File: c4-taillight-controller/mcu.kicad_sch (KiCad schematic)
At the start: 8 parts, among them J1 Conn_01x05_Pin, M1 MDBT50Q-1MV2, X1 32.768KHz

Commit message: 8/17/2026 added MCU
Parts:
- removed C2, C3: 12pF, symbol Device:C
- removed C4, C5, C6: 10uF, symbol Device:C
- removed J1: Conn_01x05_Pin, symbol Connector:Conn_01x05_Pin
- removed M1: MDBT50Q-1MV2, symbol MDBT50Q:MDBT50Q_52840
- removed X1: 32.768KHz, symbol Device:Crystal
- added C10, C11, C9: 10uF, symbol Device:C
- added C7, C8: 12pF, symbol Device:C
- added J2: Conn_01x05_Pin, symbol Connector:Conn_01x05_Pin
- added M2: MDBT50Q-1MV2, symbol MDBT50Q:MDBT50Q_52840
- added X2: 32.768KHz, symbol Device:Crystal
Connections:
- net D+: now also M2.35 (D+)
- net D-: now also M2.34 (D-)
- net GND: now also C10.2, C11.1, C7.1, C8.1, C9.1, J2.1 (Pin_1), M2.1 (GND), M2.15 (GND), M2.2 (GND), M2.33 (GND), M2.55 (GND)
- net RESET: now also J2.2 (Pin_2), M2.40 (P0.18/RESET)
- net SWDCLK: now also J2.4 (Pin_4), M2.53 (SWDCLK)
- net SWDIO: now also J2.3 (Pin_3), M2.51 (SWDIO)
- net VBUS (+5V): now also C11.2, M2.32 (VBUS)
- net VDD HV (+5V): now also C10.1, M2.30 (VDDH)
- net VDD_RF: now also C9.2, J2.5 (Pin_5), M2.28 (VDD)
- net XL1: now also C7.2, M2.17 (P0.00/XL1), X2.2
- net XL2: now also C8.2, M2.18 (P0.01/XL2), X2.1
- new net DCCH: M2.31 (DCCH)
- new net P0.02/AIN0: M2.11 (P0.02/AIN0)
- new net P0.03/AIN1: M2.9 (P0.03/AIN1)
- new net P0.04/AIN2: M2.20 (P0.04/AIN2)
- new net P0.05/AIN3: M2.21 (P0.05/AIN3)
- new net P0.06: M2.22 (P0.06)
- new net P0.07: M2.23 (P0.07)
- new net P0.08: M2.24 (P0.08)
- new net P0.09/NFC1: M2.52 (P0.09/NFC1)
- new net P0.10/NFC2: M2.54 (P0.10/NFC2)
- new net P0.11: M2.27 (P0.11)
- new net P0.12: M2.29 (P0.12)
- new net P0.13: M2.37 (P0.13)
- new net P0.14: M2.36 (P0.14)
- new net P0.15: M2.39 (P0.15)
- new net P0.16: M2.38 (P0.16)
- new net P0.17: M2.41 (P0.17)
- new net P0.19: M2.42 (P0.19)
- new net P0.20: M2.44 (P0.20)
- new net P0.21: M2.43 (P0.21)
- new net P0.22: M2.46 (P0.22)
- new net P0.23: M2.45 (P0.23)
- new net P0.24: M2.48 (P0.24)
- new net P0.25: M2.49 (P0.25)
- new net P0.26: M2.19 (P0.26)
- new net P0.27: M2.16 (P0.27)
- new net P0.28/AIN4: M2.13 (P0.28/AIN4)
- new net P0.29/AIN5: M2.10 (P0.29/AIN5)
- new net P0.30/AIN6: M2.14 (P0.30/AIN6)
- new net P0.31/AIN7: M2.12 (P0.31/AIN7)
- new net P1.00: M2.47 (P1.00)
- new net P1.01: M2.61 (P1.01)
- new net P1.02: M2.50 (P1.02)
- new net P1.03: M2.60 (P1.03)
- new net P1.04: M2.56 (P1.04)
- new net P1.05: M2.59 (P1.05)
- new net P1.06: M2.57 (P1.06)
- new net P1.07: M2.58 (P1.07)
- new net P1.08: M2.25 (P1.08)
- new net P1.09: M2.26 (P1.09)
- new net P1.10: M2.3 (P1.10)
- new net P1.11: M2.4 (P1.11)
- new net P1.12: M2.5 (P1.12)
- new net P1.13: M2.6 (P1.13)
- new net P1.14: M2.7 (P1.14)
- new net P1.15: M2.8 (P1.15)

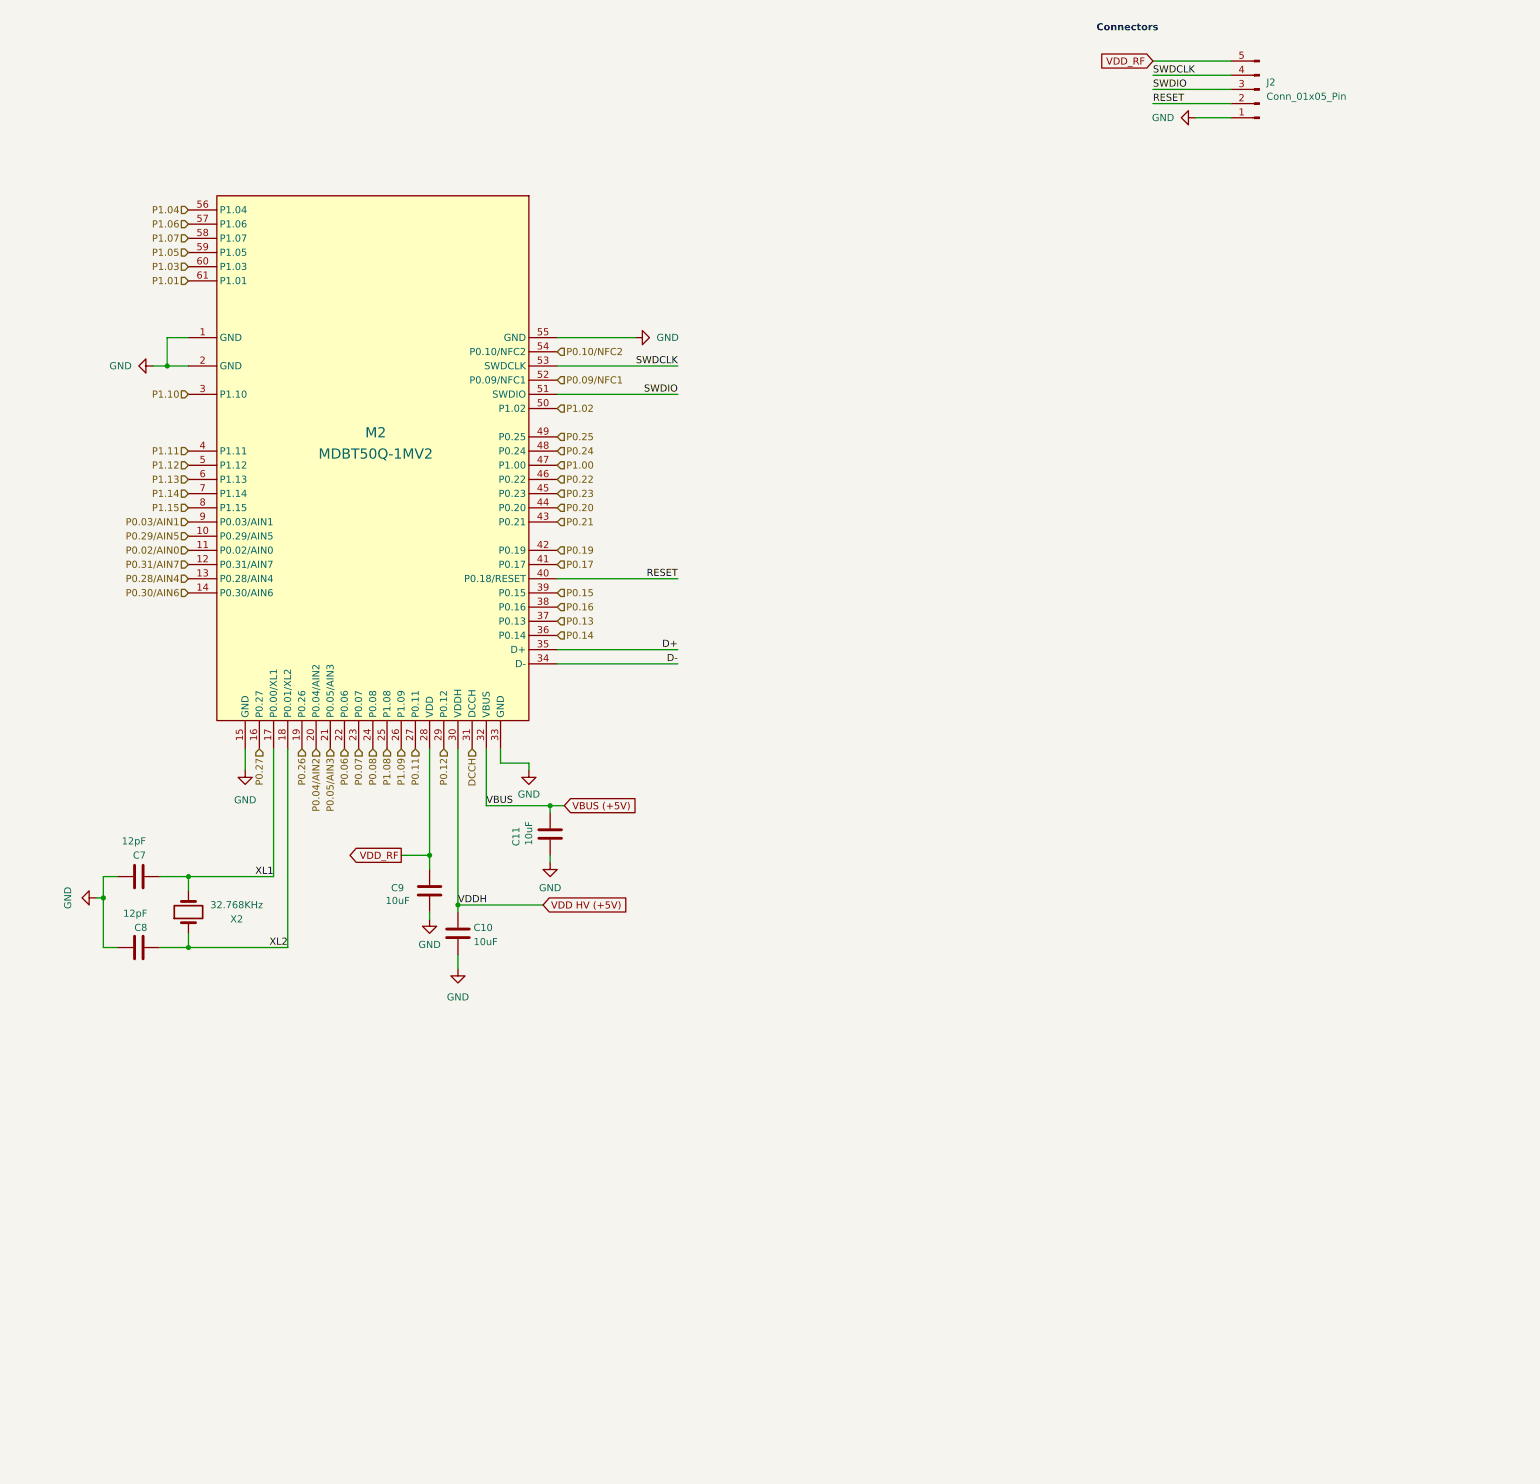
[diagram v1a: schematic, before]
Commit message: Finished complete layout of sheets
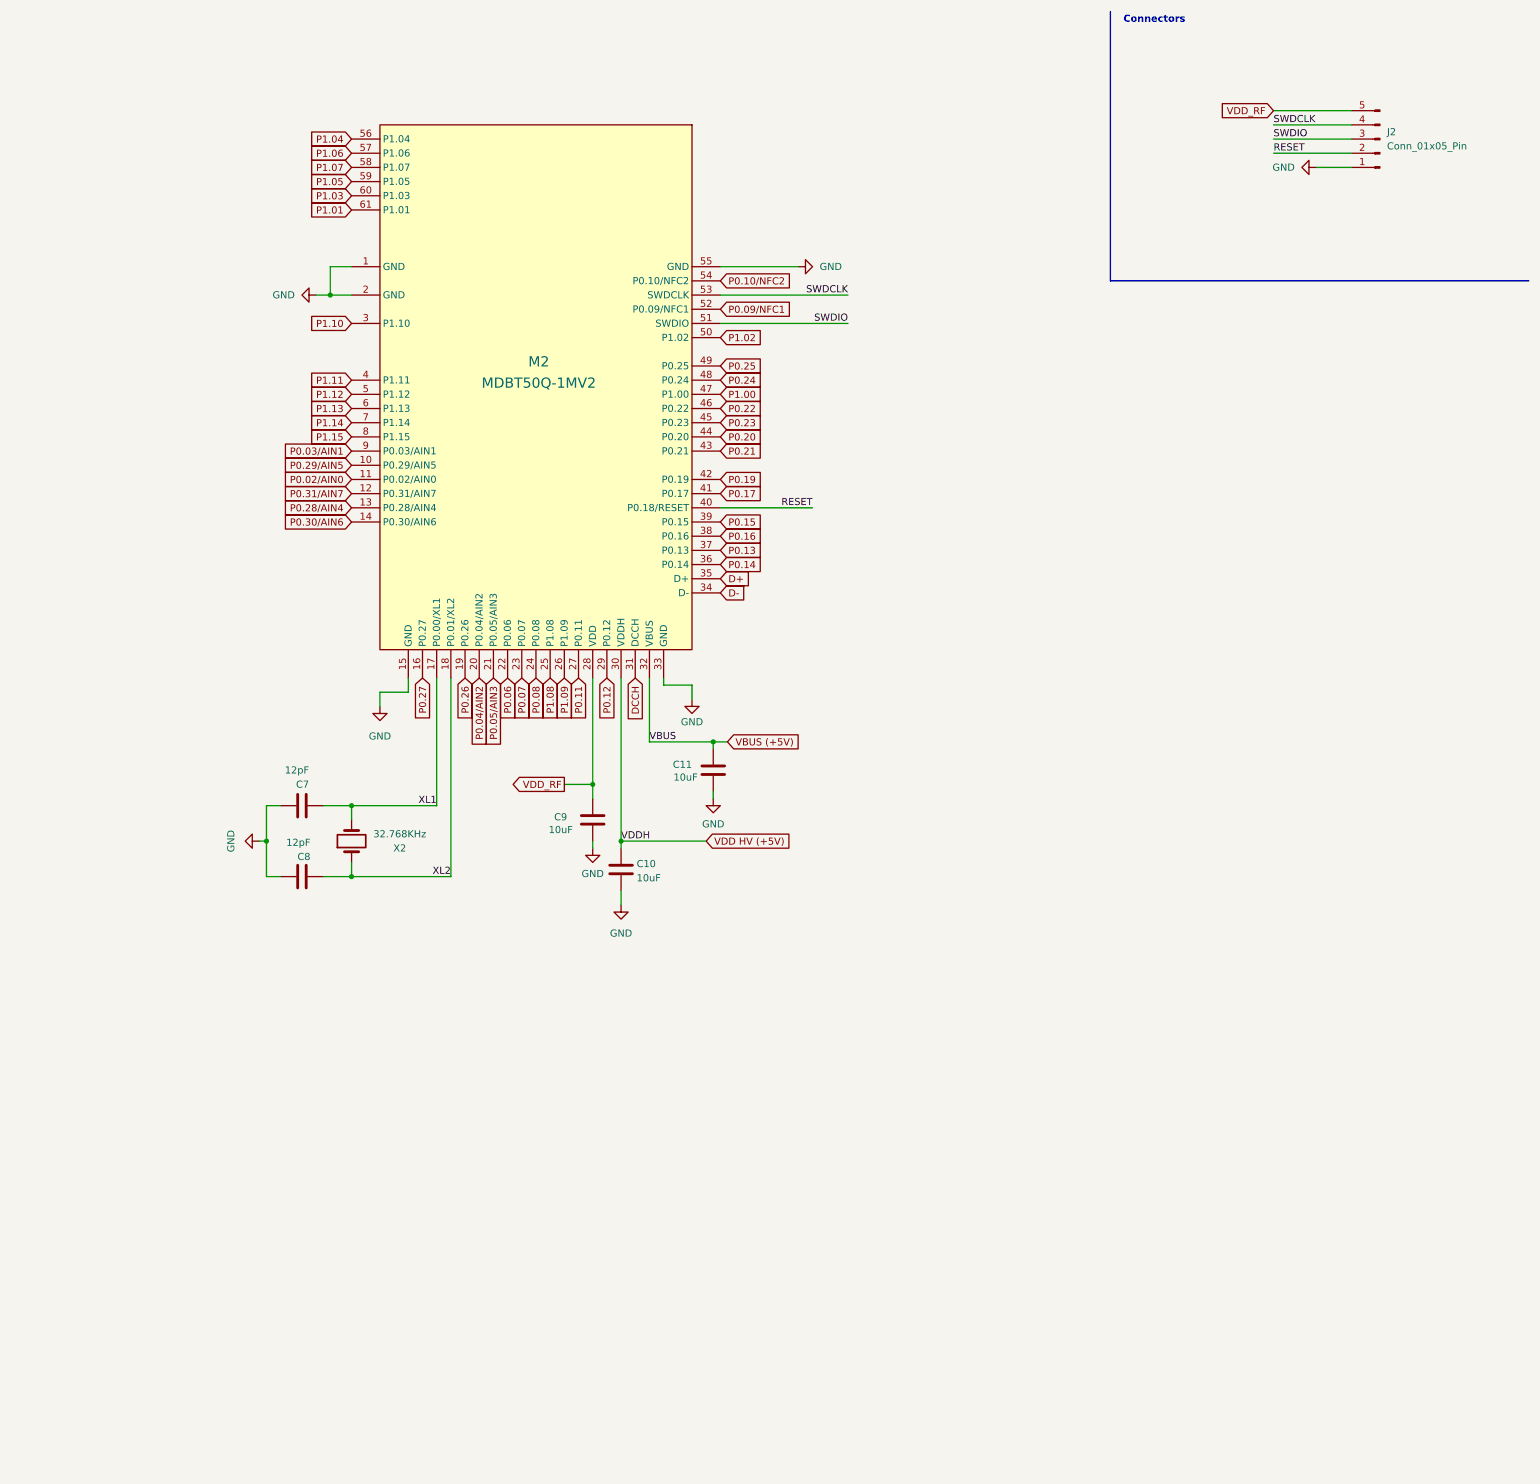
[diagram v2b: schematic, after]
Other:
- moved on the sheet: C10, C11, C7, C8, C9, J2, M2, X2
